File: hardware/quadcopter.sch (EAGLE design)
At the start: 54 parts, among them J1 HEADER-4POS-0.1IN-FEMALE-SMD-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, J2 HEADER-10POSTH-254X10, J3 HEADER-4POS-0.1IN-FEMALE, J4 AVR_SPI_PRG_6-SMD, Q1 N-MOSFET-SI2302DS, Q2 N-MOSFET-SI2302DS, Q3 N-MOSFET-SI2302DS, Q4 N-MOSFET-SI2302DS, SW1 PUSHBUTTON_-4.5X4.5, U1 ATMEGA128RFA1, U2 IMU_LSM9DS1-LSM9DS1, Y1 CRYSTAL5X3

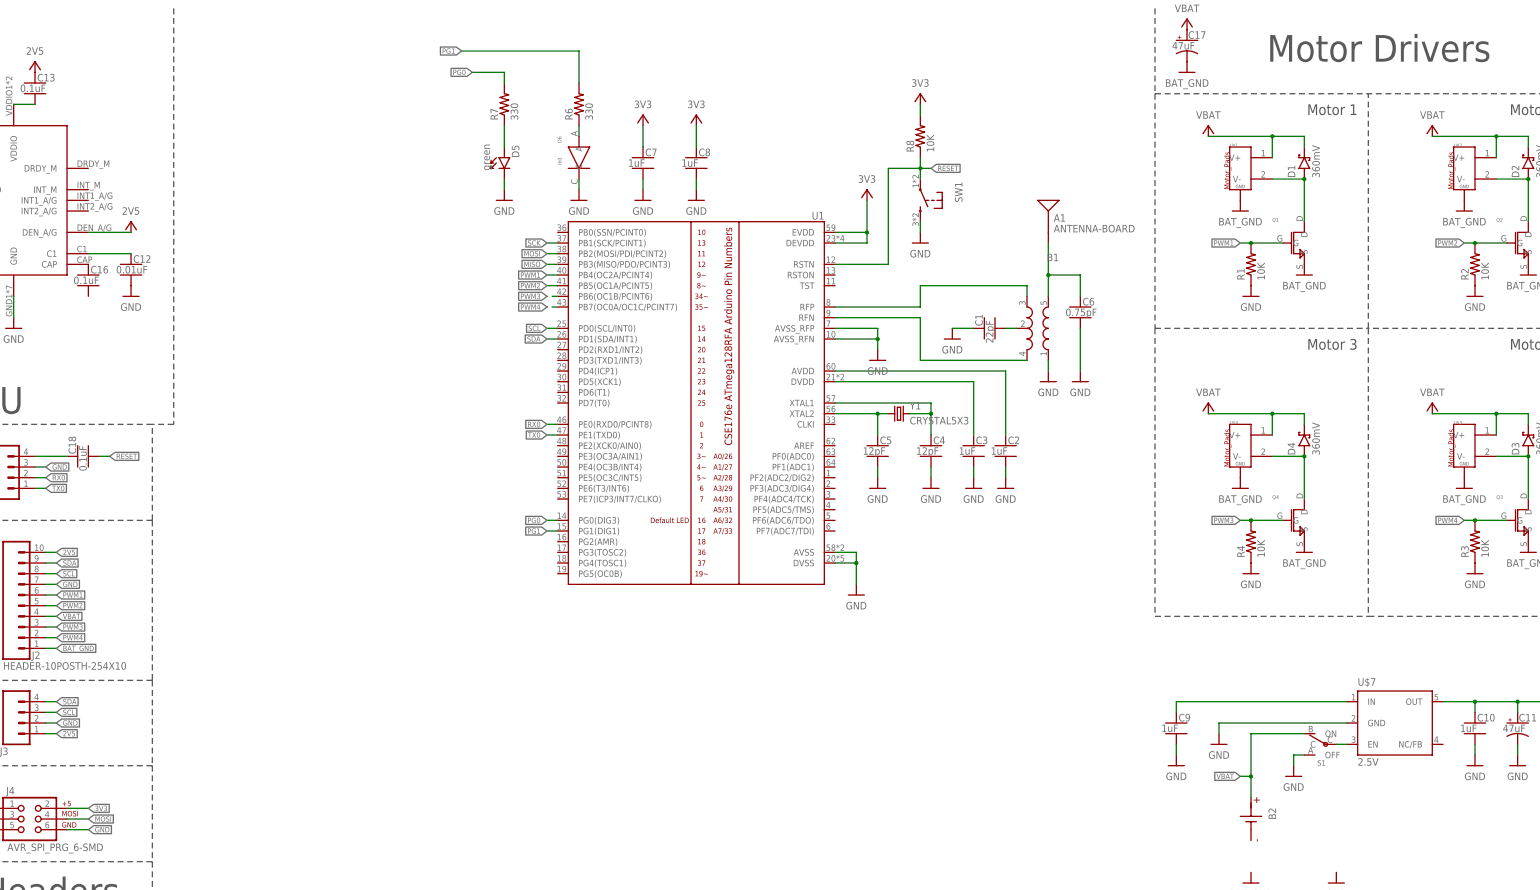
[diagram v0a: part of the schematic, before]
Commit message: Replaced 3V3 with 2V5 and added GND to IMU cap pin
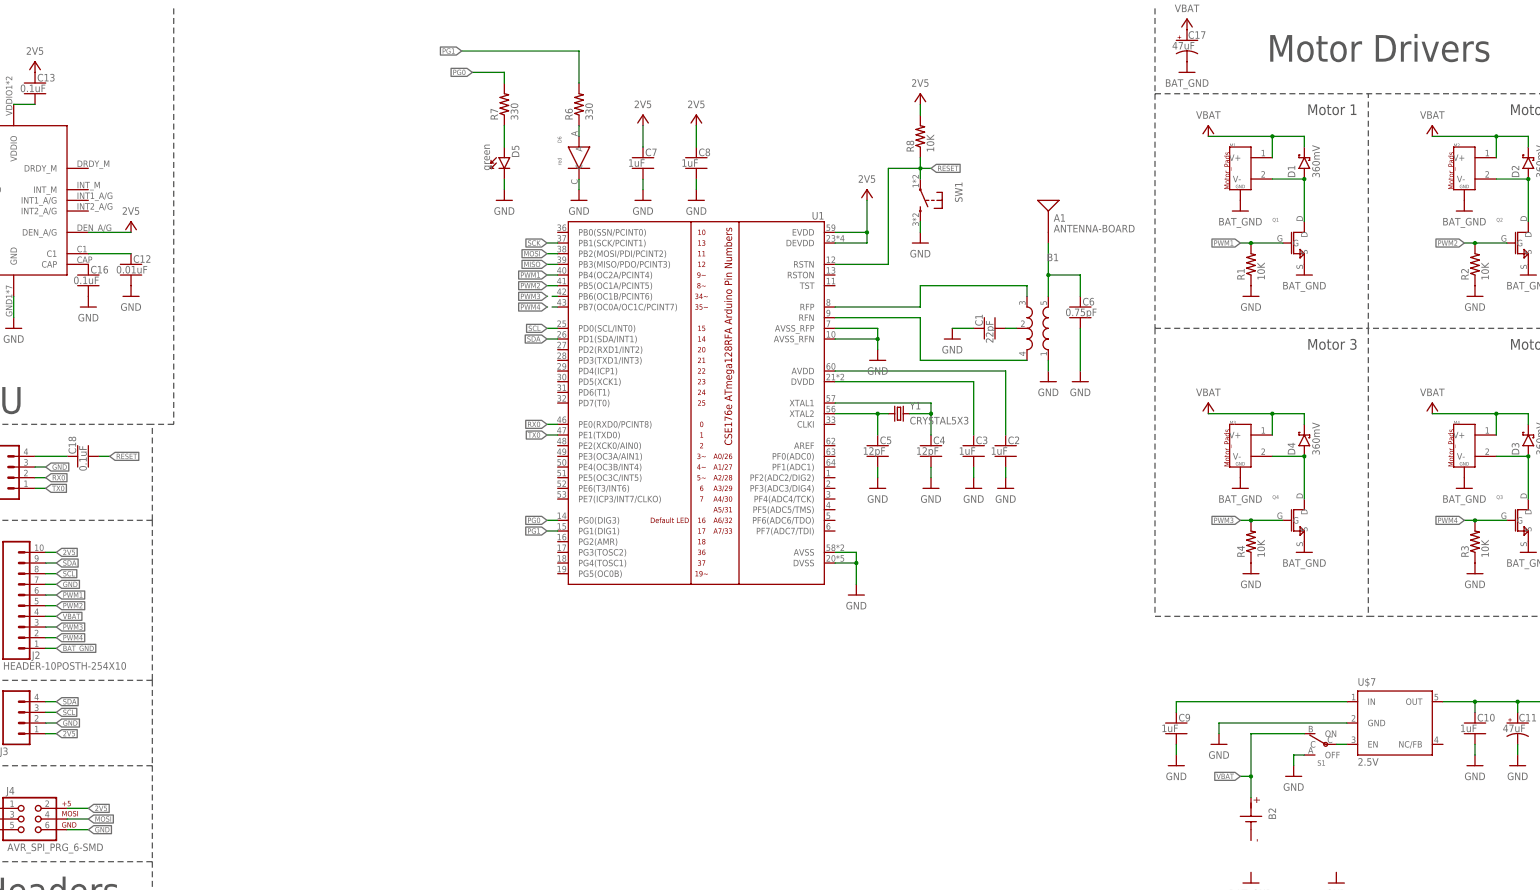
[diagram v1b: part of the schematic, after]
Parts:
- renumbered U$1 to M1, U$2 to M2, U$3 to M4, U$4 to M3
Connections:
- removed net 3V3: C7.1, C8.1, J4.2, R8.2, U1.DEVDD, U1.EVDD
- net 2V5: now also C7.1, C8.1, J4.2, R8.2, U1.DEVDD, U1.EVDD
- net GND: now also C16.2

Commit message: Initial Submit
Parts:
- added U$12: NET_BRIDGE_5X5, custom:NET_BRIDGE_5X5
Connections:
- removed net N$16: C9.1, U$7.IN
- net BAT_GND: now also B2.N, U$12.1
- net GND: now also U$12.2
- net VBAT: now also C9.1, U$7.IN
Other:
- moved on the sheet: B2, C9, S1

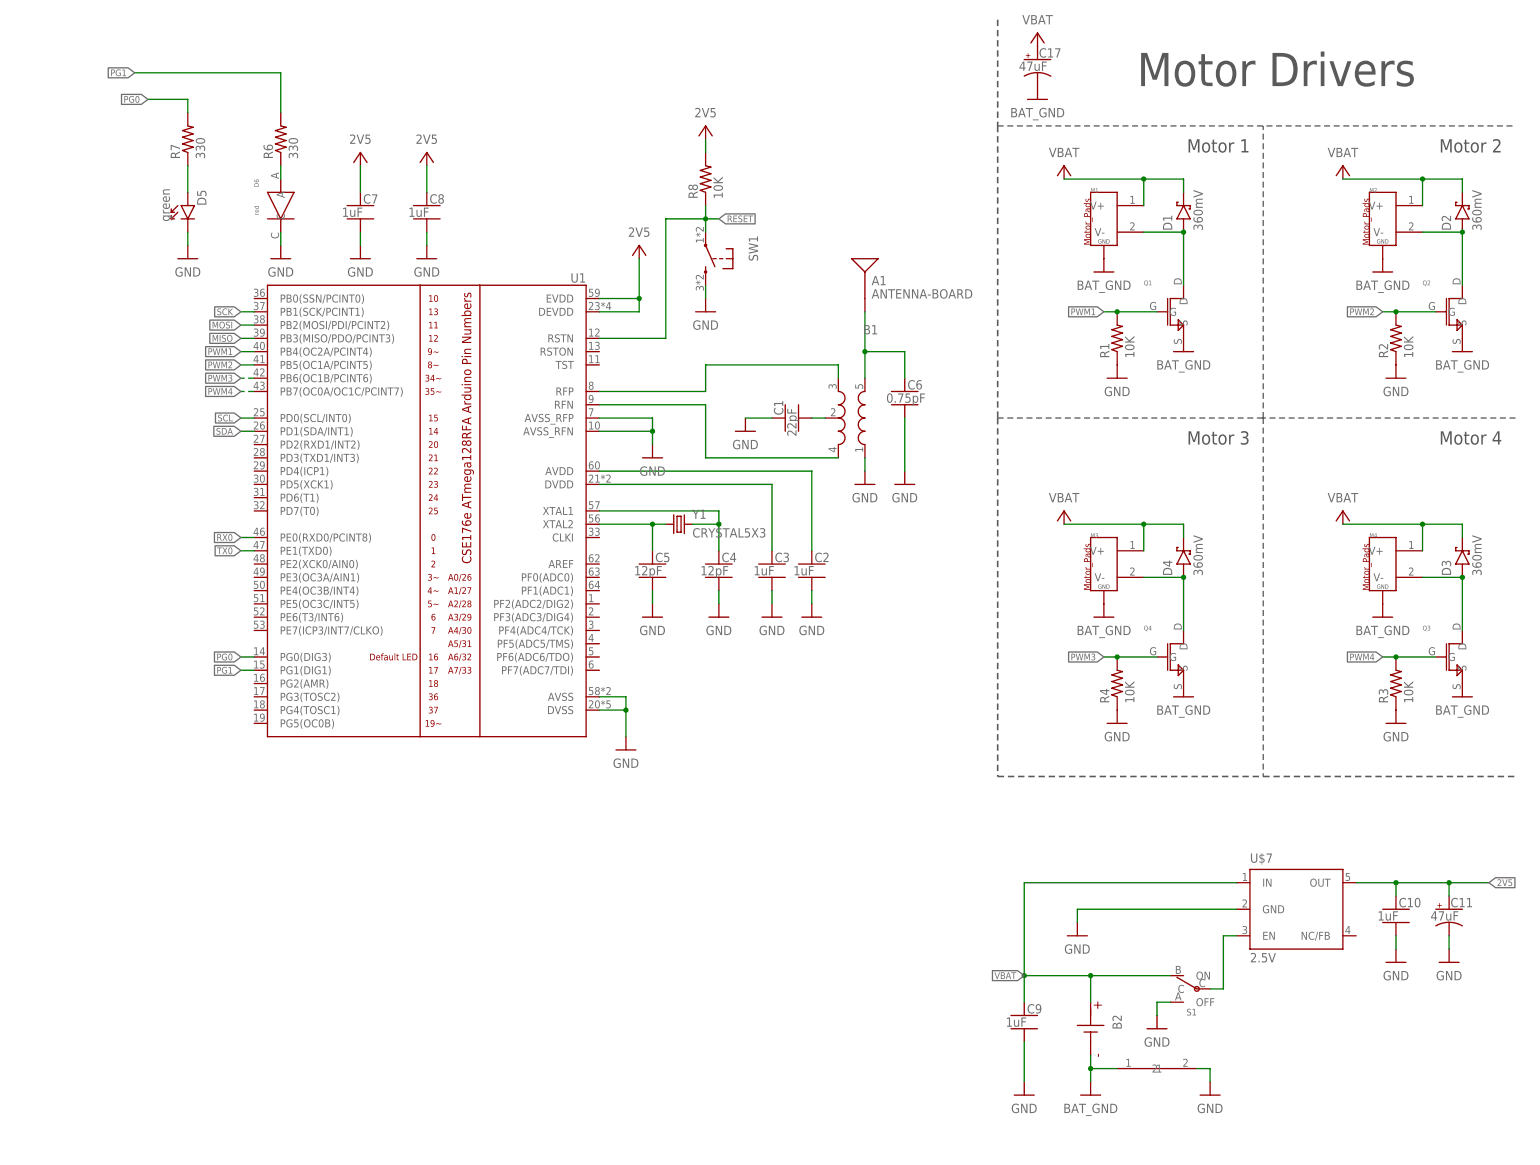
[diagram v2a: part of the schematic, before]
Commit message: Renamed parts that had $ symbols in them
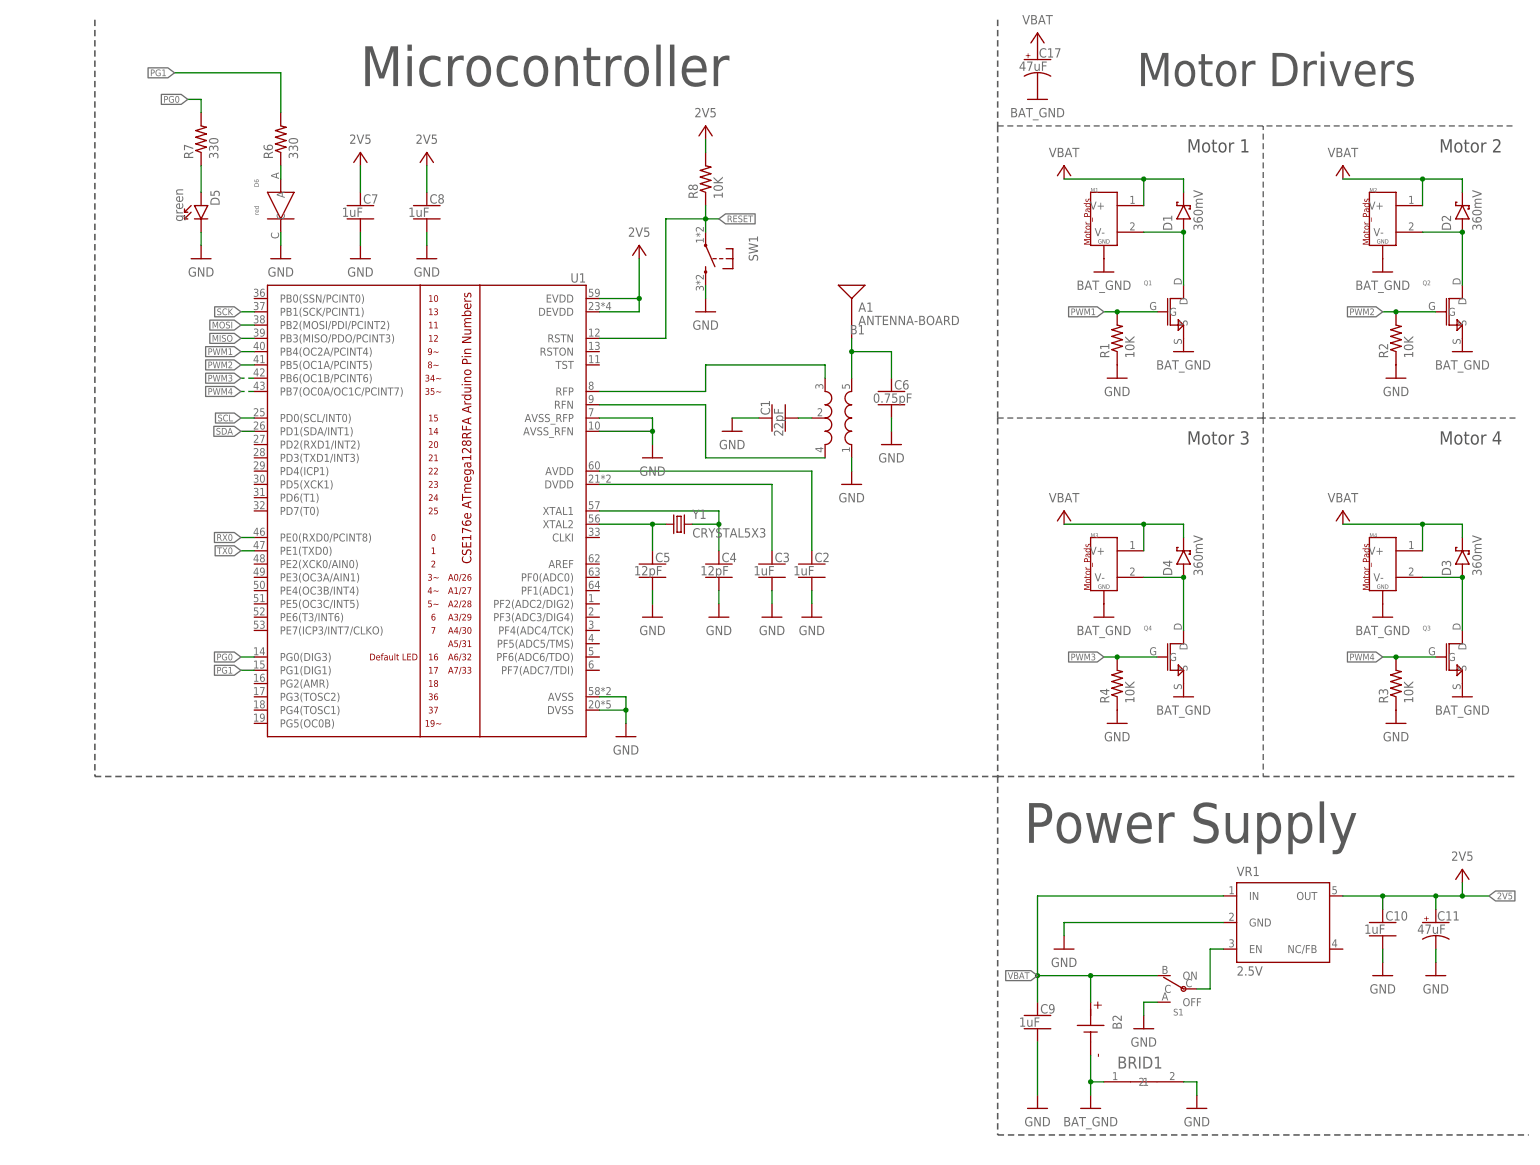
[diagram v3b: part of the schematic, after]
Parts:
- removed U$12: NET_BRIDGE_5X5, custom:NET_BRIDGE_5X5
- removed U$7: 2.5V, quadparts_prebuilt:TPS73633-DBVT2.5V
- added BRID1: NET_BRIDGE_5X5, custom:NET_BRIDGE_5X5
- added VR1: 2.5V, quadparts_prebuilt:TPS73633-DBVT2.5V
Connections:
- net 2V5: now also VR1.OUT; no longer U$7.OUT
- net BAT_GND: now also BRID1.1; no longer U$12.1
- net GND: now also BRID1.2, VR1.GND; no longer U$12.2, U$7.GND
- net N$23: now also VR1.EN; no longer U$7.EN
- net VBAT: now also VR1.IN; no longer U$7.IN
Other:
- note added: "Microcontroller"
- note added: "Power Supply"
- moved on the sheet: A1, B1, C1, C10, C11, C6, C9, D5, R7, S1

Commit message: Replace `quadparts_prebuilt` with `quadparts_prebuilt_2022`
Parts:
- removed R8: 10K, quadparts_prebuilt:RESISTOR_SMD-2012-0805-10K
- added R5: 330, quadparts_prebuilt_2022:RESISTOR_SMD-2012-0805-330
- A1: device quadparts_prebuilt:ANTENNA-BOARD -> quadparts_prebuilt_2022:ANTENNA-BOARD
- B1: device quadparts_prebuilt:BALUN0805 -> quadparts_prebuilt_2022:BALUN0805
- B2: device quadparts_prebuilt:BATTERY-SMD -> quadparts_prebuilt_2022:BATTERY-SMD
- C1: device quadparts_prebuilt:CAPACITOR-NP_SMD-0603_CERAMIC-22PF -> quadparts_prebuilt_2022:CAPACITOR-NP_SMD-2012-0805_CERAMIC-22PF
- C10, C2, C3, C9: device quadparts_prebuilt:CAPACITOR-NP_SMD-2012-0805_CERAMIC-1UF -> quadparts_prebuilt_2022:CAPACITOR-NP_SMD-2012-0805_CERAMIC-1UF
- C11: device quadparts_prebuilt:CAPACITOR-POL_47UF-SMD-1206-TAJA -> quadparts_prebuilt_2022:CAPACITOR-POL_47UF-SMD-1206-TAJA
- C4, C5: device quadparts_prebuilt:CAPACITOR-NP_SMD-2012-0805_CERAMIC-12PF -> quadparts_prebuilt_2022:CAPACITOR-NP_SMD-2012-0805_CERAMIC-12PF
- C6: device quadparts_prebuilt:CAPACITOR-NP_SMD-0603_CERAMIC-0.75PF -> quadparts_prebuilt_2022:CAPACITOR-NP_SMD-2012-0805_CERAMIC-0.75PF
- C7, C8: device quadparts_prebuilt:CAPACITOR-NP_SMD-0603_CERAMIC-1UF -> quadparts_prebuilt_2022:CAPACITOR-NP_SMD-2012-0805_CERAMIC-1UF
- D5: device quadparts_prebuilt:DIODE-LED_SMD-2012-0805-GREEN -> quadparts_prebuilt_2022:DIODE-LED_SMD-2012-0805-GREEN
- R6: device quadparts_prebuilt:RESISTOR_SMD-2012-0805-330 -> quadparts_prebuilt_2022:RESISTOR_SMD-2012-0805-330
- R7: value 330 -> 10K; device quadparts_prebuilt:RESISTOR_SMD-2012-0805-330 -> quadparts_prebuilt_2022:RESISTOR_SMD-2012-0805-10K
- S1: device quadparts_prebuilt:POWER-SWITCH-MFS201N-9-Z-SMD-EDGE -> quadparts_prebuilt_2022:POWER-SWITCH-MFS201N-9-Z-SMD-EDGE
- SW1: device quadparts_prebuilt:PUSHBUTTON_-4.5X4.5 -> quadparts_prebuilt_2022:PUSHBUTTON_-4.5X4.5
- U1: device quadparts_prebuilt:ATMEGA128RFA1 -> quadparts_prebuilt_2022:ATMEGA128RFA1
- VR1: device quadparts_prebuilt:TPS73633-DBVT2.5V -> quadparts_prebuilt_2022:TPS73633-DBVT2.5V
- Y1: device quadparts_prebuilt:CRYSTAL5X3 -> quadparts_prebuilt_2022:CRYSTAL5X3
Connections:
- net 2V5: now also R7.2; no longer R8.2
- net N$13: now also R6.1; no longer R7.1
- net N$5: now also R5.1; no longer R6.1
- net PG0: now also R6.2; no longer R7.2
- net PG1: now also R5.2; no longer R6.2
- net RESET: now also R7.1; no longer R8.1
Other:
- moved on the sheet: R6, R7

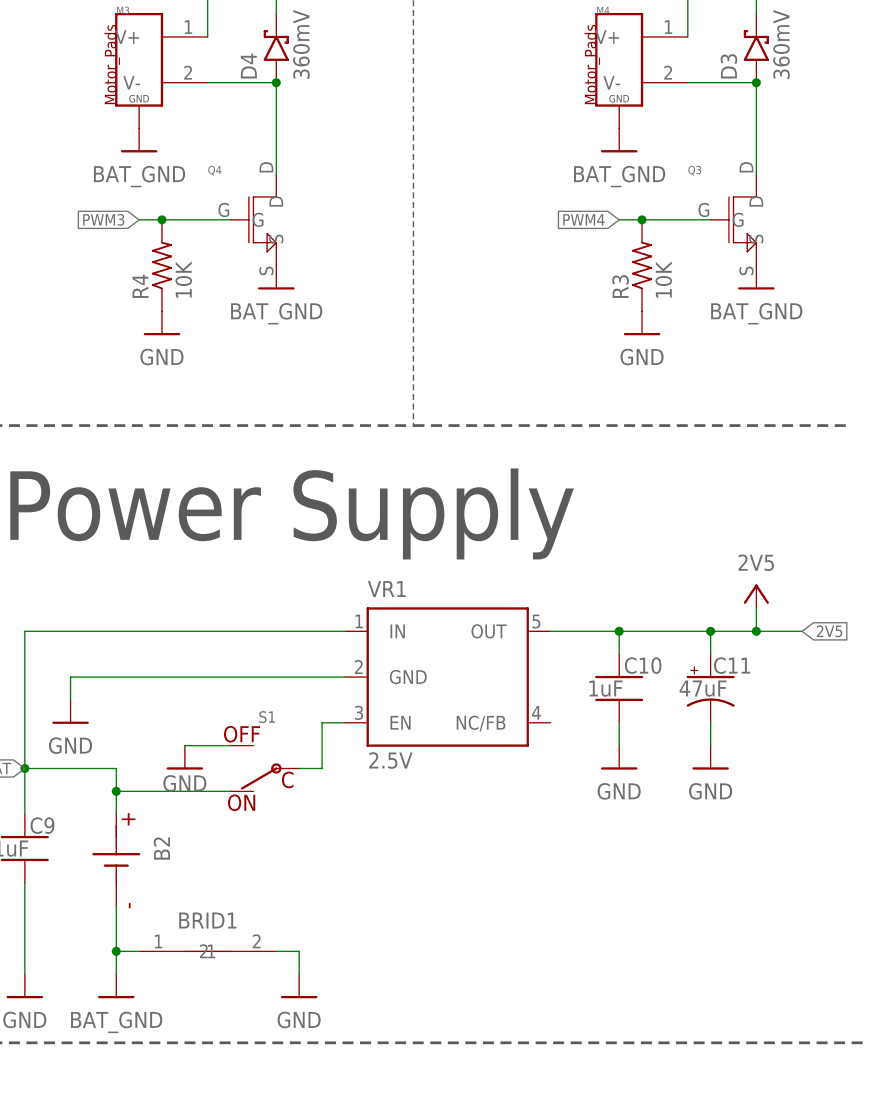
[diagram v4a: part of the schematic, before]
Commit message: Use parts in local custom library
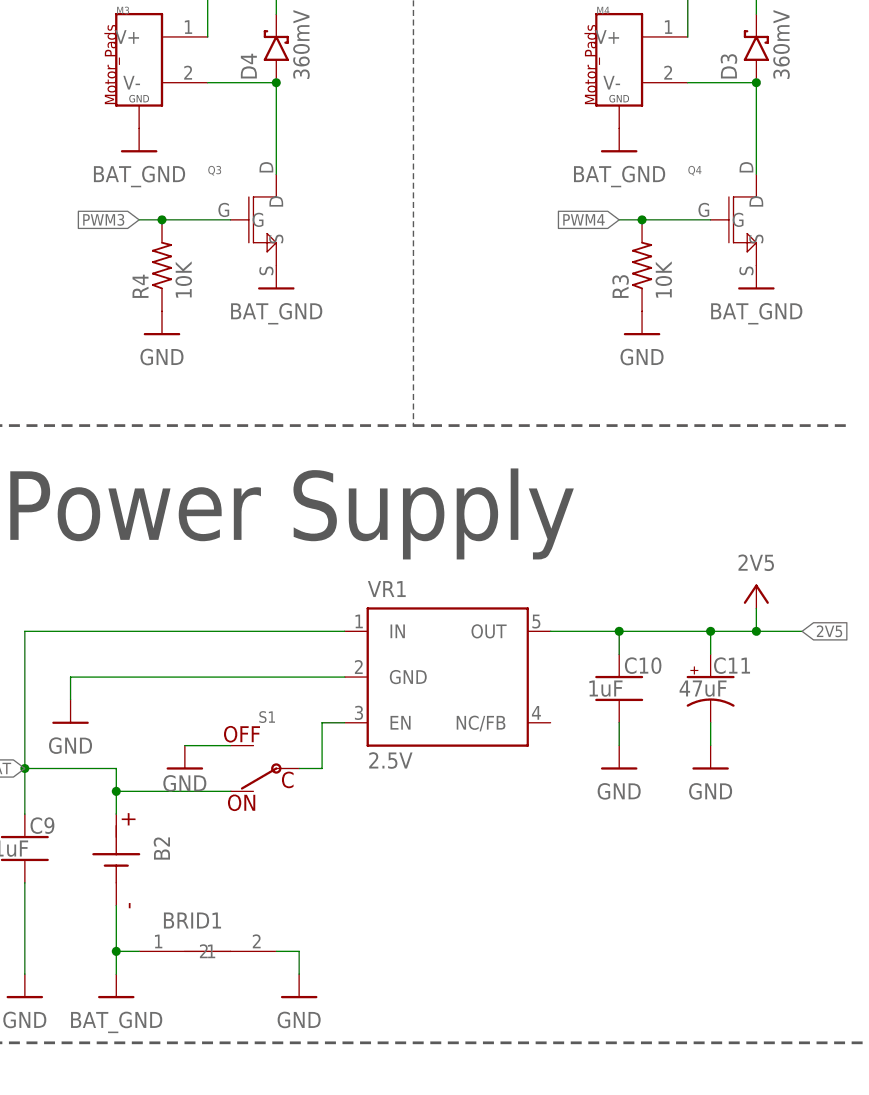
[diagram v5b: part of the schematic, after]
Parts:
- BRID1: device custom:NET_BRIDGE_5X5 -> custom_michael_shao:NET_BRIDGE_5X5
- D6: device custom:LED_RED-LTST-C170EKT -> custom_michael_shao:LED_RED-LTST-C170EKT
- Q1, Q2, Q3, Q4: device custom:N-MOSFET-SI2302DS -> custom_michael_shao:N-MOSFET-SI2302DS
- U2: device custom:IMU_LSM9DS1-LSM9DS1 -> custom_michael_shao:IMU_LSM9DS1-LSM9DS1
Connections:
- net N$3: now also Q3.D; no longer Q4.D
- net N$4: now also Q4.D; no longer Q3.D
- net PWM3: now also Q3.G; no longer Q4.G
- net PWM4: now also Q4.G; no longer Q3.G
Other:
- moved on the sheet: Q3, Q4
